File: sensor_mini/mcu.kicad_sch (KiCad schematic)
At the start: 13 parts, among them J2 Programming Header, U8 PIC18LF26K83, U9 MCP2562, Y1 Crystal

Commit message: Clean Up
Removed old files
Cleaned up Schematics
Created new PDFs
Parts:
- renumbered C15 to C1, C16 to C2, C17 to C3, C18 to C4, J2 to J1, R3 to R1, R4 to R2, R5 to R3, R6 to R4, U8 to U1, U9 to U2
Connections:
- no-connect marks 0 -> 9
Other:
- moved on the sheet: C1, C2, C3, C4, D1, J1, R1, R2, R3, R4, U1, U2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

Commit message: Finish Analog Sensors Schematic
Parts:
- C1: value 0.1uF -> C
- C2: renamed from C4; value 10uF -> C
- C3: renamed from C2; value 27pF -> C
- C4: renamed from C3; value 27pF -> C
- J1: value Programming Header -> Conn_01x05_Female-Connector
- R1, R2, R3: value 10K -> R_US
- R4: value 330R -> R_US
- U1: value PIC18LF26K83 -> PIC18F26K83
- U2: value MCP2562 -> MCP2562-canhw-sensors-rescue-sensors-rescue-sensors-rescue
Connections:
- net SENSOR1_AMP_CAPABLE: now reaches U1.6 (RA4)
- net SENSOR2_AMP_CAPABLE: now reaches U1.7 (RA5)
- net CURR_INPUT_12V renamed SENSOR4_REGULAR
- net PRESSURE renamed SENSOR3_REGULAR
- no-connect marks 9 -> 7
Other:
- moved on the sheet: C1, D1, R1, R2, R3, R4, U1

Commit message: Finish digital sensors schematic
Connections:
- net INT_IMU: no longer names the net of U1.12 (RC1)
- net INT_MAG: no longer names the net of U1.13 (RC2)
- no-connect marks 7 -> 9
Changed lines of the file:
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@@
   (junction (at 233.68 129.54) (diameter 0) (color 0 0 0 0)
   )
+  (no_connect (at 88.9 135.89))
   (no_connect (at 125.73 120.65))
   (no_connect (at 125.73 115.57))
@@
   (no_connect (at 125.73 130.81))
   (no_connect (at 88.9 130.81))
+  (no_connect (at 88.9 133.35))
   (wire (pts (xy 60.96 135.89) (xy 60.96 138.43))
     (stroke (width 0) (type default) (color 0 0 0 0))
   )
-  (wire (pts (xy 88.9 133.35) (xy 81.28 133.35))
-    (stroke (width 0) (type default) (color 0 0 0 0))
-  )
   (wire (pts (xy 215.9 46.99) (xy 223.52 46.99))
     (stroke (width 0) (type default) (color 0 0 0 0))
@@
   )
   (wire (pts (xy 80.645 116.84) (xy 51.435 116.84))
-    (stroke (width 0) (type default) (color 0 0 0 0))
-  )
-  (wire (pts (xy 88.9 135.89) (xy 81.28 135.89))
     (stroke (width 0) (type default) (color 0 0 0 0))
   )
@@
     (effects (font (size 1.27 1.27)) (justify right))
   )
-  (hierarchical_label "INT_IMU" (shape input) (at 81.28 133.35 180)
-    (effects (font (size 1.27 1.27)) (justify right))
-  )
-  (hierarchical_label "INT_MAG" (shape input) (at 81.28 135.89 180)
-    (effects (font (size 1.27 1.27)) (justify right))
-  )

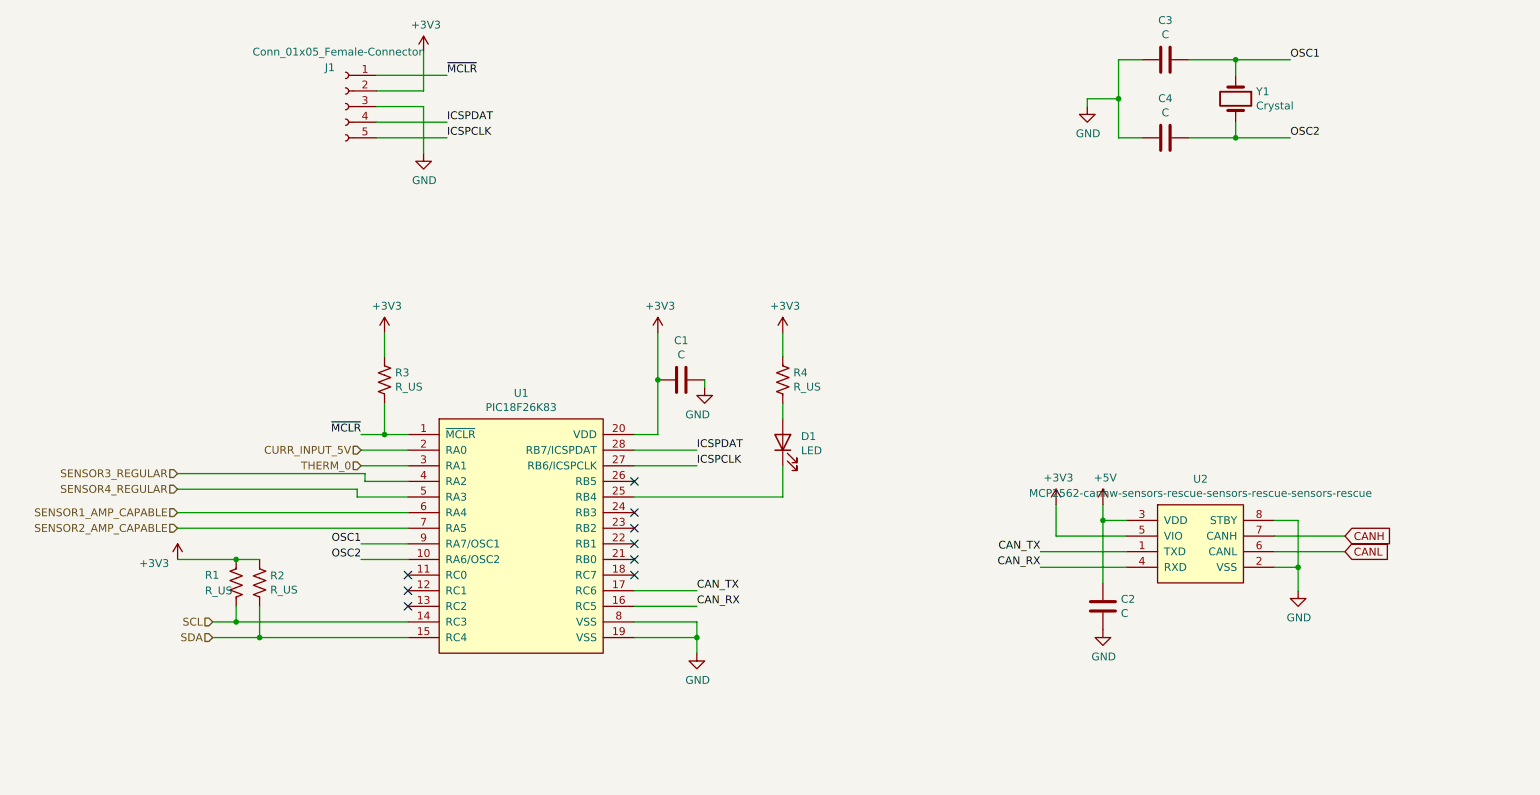
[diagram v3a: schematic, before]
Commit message: Added Test Points For the People
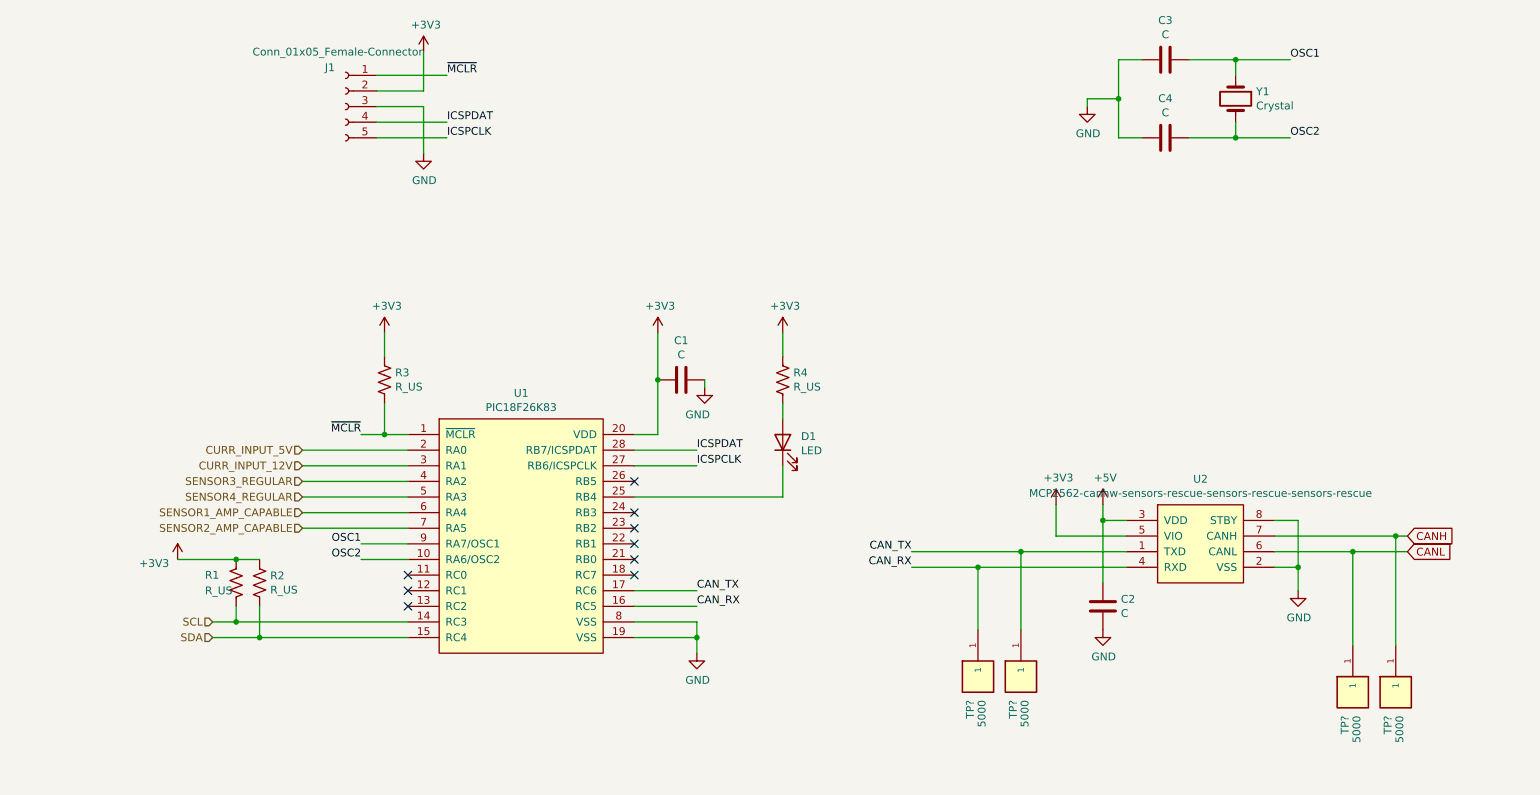
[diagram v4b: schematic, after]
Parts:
- added TP? (x4): 5000, KEYSTONE_5000, symbol Keysight_5000_testpoints:5000
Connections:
- net CANH: now also TP?.1
- net CANL: now also TP?.1
- net CAN_RX: now also TP?.1
- net CAN_TX: now also TP?.1
- net THERM_0 renamed CURR_INPUT_12V

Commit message: Clean up the festering cesspool that was the minisensor folder
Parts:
- J1: symbol sensors-rescue:Conn_01x05_Female-Connector -> Connector:Conn_01x05_Female
- U2: value MCP2562-canhw-sensors-rescue-sensors-rescue-sensors-rescue -> MC2562; symbol sensors-rescue:MCP2562-canhw-sensors-rescue-sensors-rescue-sensors-rescue -> canhw:MCP2562
- gave numbers to parts that had none: 4
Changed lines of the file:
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@@
     (pin "1")
   )
-  (symbol (lib_id "sensors-rescue:MCP2562-canhw-sensors-rescue-sensors-rescue-sensors-rescue") (at 218.44 121.92 0) (unit 1)
+  (symbol (lib_id "canhw:MCP2562") (at 218.44 121.92 0) (unit 1)
     (in_bom yes) (on_board yes)
     (property "Reference" "U2" (id 0) (at 217.805 115.189 0))
-    (property "Value" "MCP2562-canhw-sensors-rescue-sensors-rescue-sensors-rescue" (id 1) (at 217.805 117.5004 0))
+    (property "Value" "MC2562" (id 1) (at 217.805 117.5004 0))
     (property "Footprint" "Package_SO:SOIC-8_3.9x4.9mm_P1.27mm" (id 2) (at 218.44 121.92 0)
       (effects (font (size 1.27 1.27)) hide)
     )
-    (property "Datasheet" "" (id 3) (at 218.44 121.92 0)
+    (property "Datasheet" "http://hades.mech.northwestern.edu/images/5/5e/MCP2562.pdf" (id 3) (at 218.44 121.92 0)
       (effects (font (size 1.27 1.27)) hide)
     )
@@
     (pin "1")
   )
-  (symbol (lib_id "sensors-rescue:Conn_01x05_Female-Connector") (at 78.74 54.61 0) (mirror y) (unit 1)
+  (symbol (lib_id "Connector:Conn_01x05_Female") (at 78.74 54.61 0) (mirror y) (unit 1)
     (in_bom yes) (on_board yes)
     (property "Reference" "J1" (id 0) (at 76.2 48.26 0))
@@
   (symbol (lib_id "Keysight_5000_testpoints:5000") (at 181.61 147.32 270) (unit 1)
     (in_bom yes) (on_board yes)
-    (property "Reference" "TP?" (id 0) (at 180.34 151.13 0)
+    (property "Reference" "TP1" (id 0) (at 180.34 151.13 0)
       (effects (font (size 1.27 1.27)) (justify left))
     )
@@
   (symbol (lib_id "Keysight_5000_testpoints:5000") (at 242.57 149.86 270) (unit 1)
     (in_bom yes) (on_board yes)
-    (property "Reference" "TP?" (id 0) (at 241.3 153.67 0)
+    (property "Reference" "TP3" (id 0) (at 241.3 153.67 0)
       (effects (font (size 1.27 1.27)) (justify left))
     )
@@
   (symbol (lib_id "Keysight_5000_testpoints:5000") (at 188.595 147.32 270) (unit 1)
     (in_bom yes) (on_board yes)
-    (property "Reference" "TP?" (id 0) (at 187.325 151.13 0)
+    (property "Reference" "TP2" (id 0) (at 187.325 151.13 0)
       (effects (font (size 1.27 1.27)) (justify left))
     )
@@
   (symbol (lib_id "Keysight_5000_testpoints:5000") (at 249.555 149.86 270) (unit 1)
     (in_bom yes) (on_board yes)
-    (property "Reference" "TP?" (id 0) (at 248.285 153.67 0)
-      (effects (font (size 1.27 1.27)) (justify left))
-    )
+    (property "Reference" "TP4" (id 0) (at 248.285 153.67 0)
+      (effects (font (size 1.27 1.27)) (justify left))
+    )

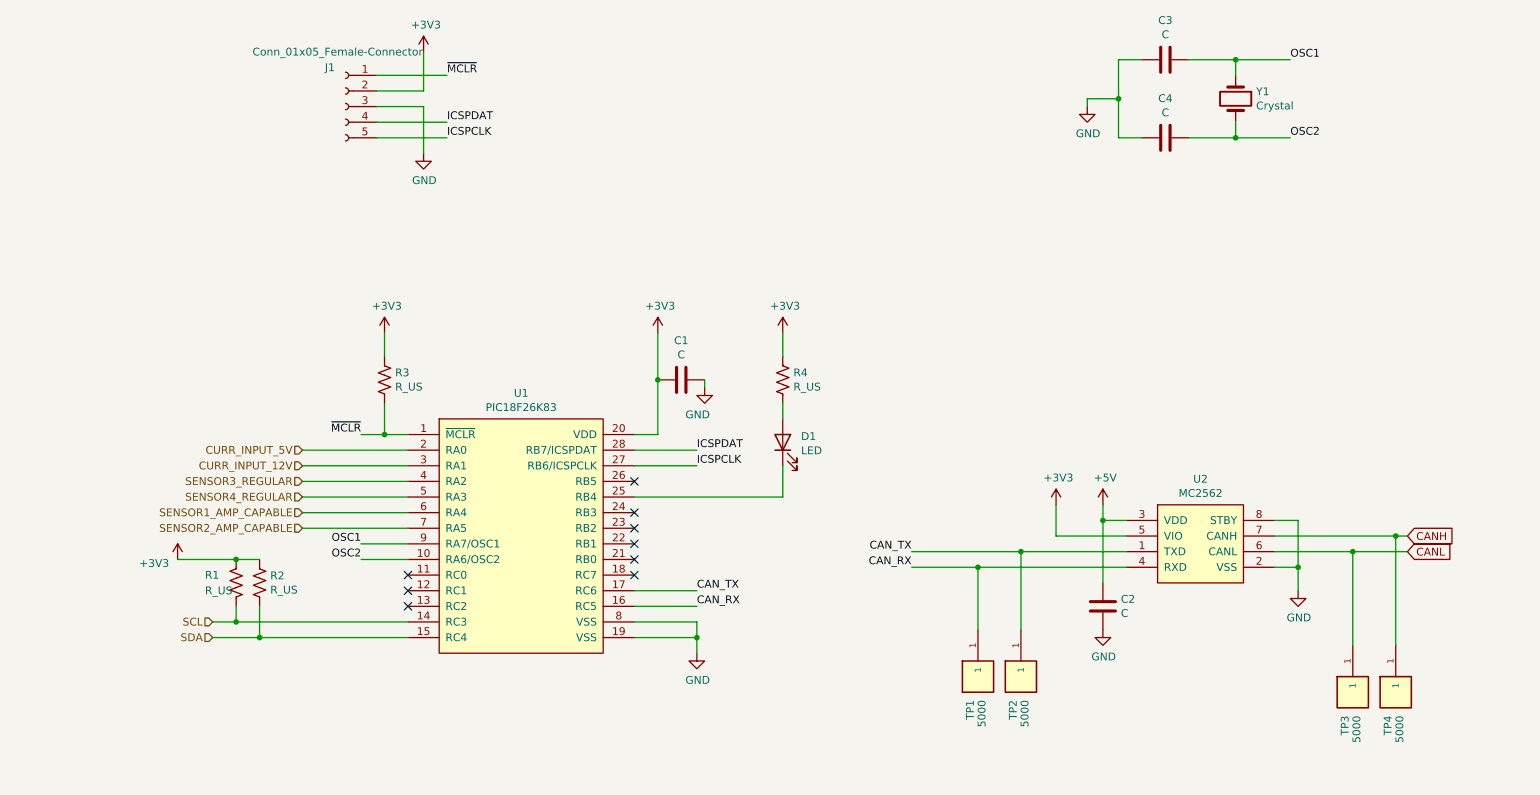
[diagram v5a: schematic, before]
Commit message: Begin addressing PR comments
Added values, replaced 5->3.3regulator, added decoupling caps, fixed barometer address, accommodated 3-pin connectors, added LEDs, addedd interrupt pin, changed inductor formatting
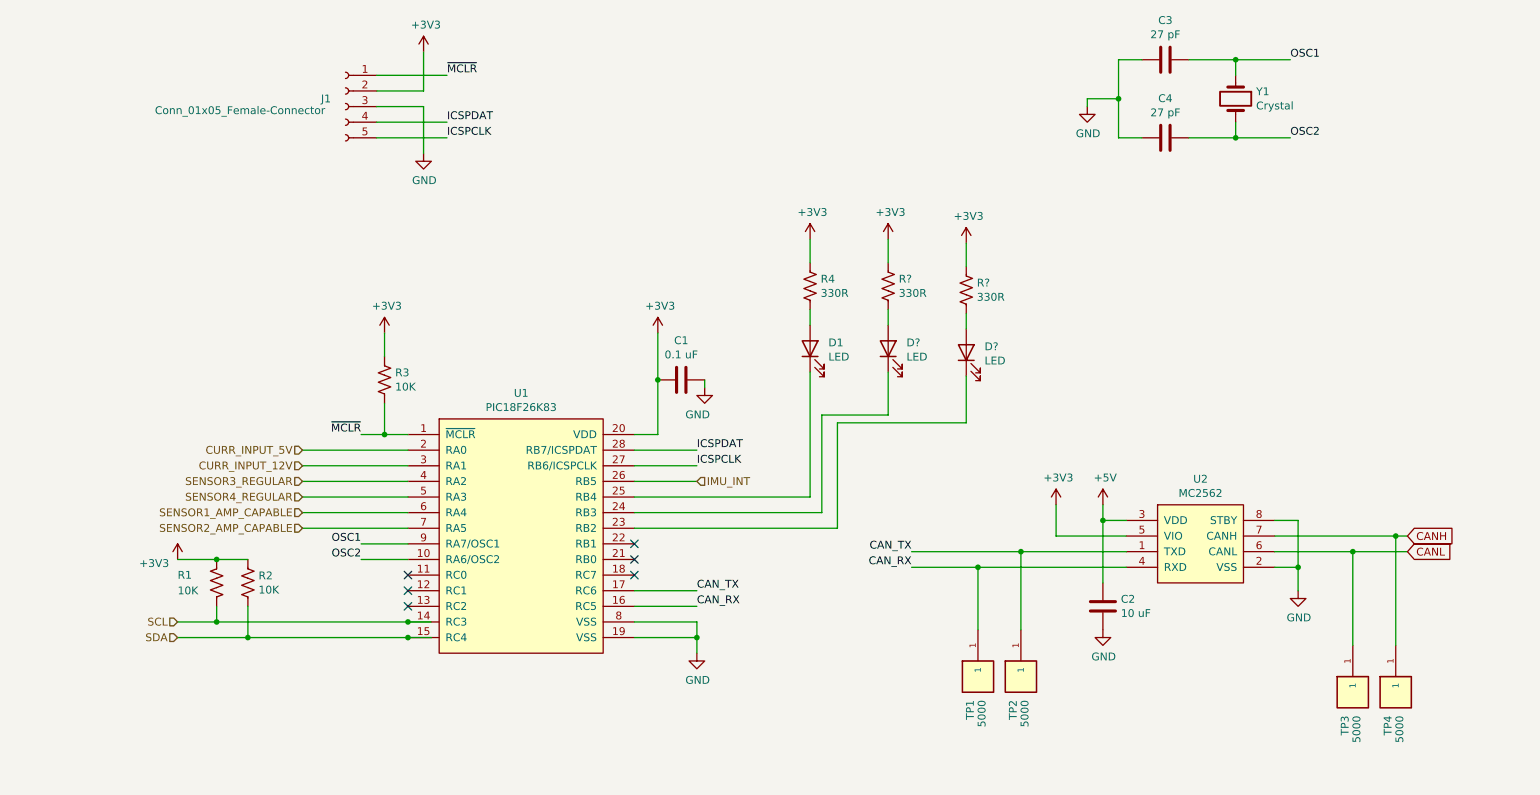
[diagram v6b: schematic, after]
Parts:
- added D? (x2): LED, LED_SMD:LED_1206_3216Metric_Pad1.42x1.75mm_HandSolder, symbol Device:LED
- added R? (x2): 330R, Resistor_SMD:R_0805_2012Metric_Pad1.15x1.40mm_HandSolder, symbol Device:R_US
- C1: value C -> 0.1 uF
- C2: value C -> 10 uF
- C3, C4: value C -> 27 pF
- R1, R2, R3: value R_US -> 10K
- R4: value R_US -> 330R
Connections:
- net +3V3: now also R?.1, R?.1
- net at U1.23 (RB2): now also D?.1 (K)
- net at U1.24 (RB3): now also D?.1 (K)
- net IMU_INT: now reaches U1.26 (RB5)
- new net: D?.2 (A), R?.2 (x2)
- no-connect marks 9 -> 6
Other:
- moved on the sheet: D1, R1, R2, R4

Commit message: Continue addressing PR comments
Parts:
- D1: value LED -> LED_RED
- D?: value LED -> LED_WHITE
- D?: value LED -> LED_BLUE
- U1: footprint Package_SO:SSOP-28_5.3x10.2mm_P0.65mm -> Package_SO:SOIC-28W_7.5x17.9mm_P1.27mm
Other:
- moved on the sheet: C1, D?, R?

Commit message: Finish addressing PR comments
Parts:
- removed TP1, TP2, TP3, TP4: 5000, KEYSTONE_5000, symbol Keysight_5000_testpoints:5000
- added TP1: TP_CANRX, canhw_footprints:KEYSTONE_5000, symbol canhw:TestPointKeystone
- added TP2: TP_CANTX, canhw_footprints:KEYSTONE_5000, symbol canhw:TestPointKeystone
- added TP3: TP_CANH, canhw_footprints:KEYSTONE_5000, symbol canhw:TestPointKeystone
- added TP4: TP_CANL, canhw_footprints:KEYSTONE_5000, symbol canhw:TestPointKeystone
- D1: value LED_RED -> LED_GREEN
- gave numbers to parts that had none: 4
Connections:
- net CANH: now also TP4.1
- net CANL: now also TP3.1
- net CAN_RX: now also TP1.1
- net CAN_TX: now also TP2.1
